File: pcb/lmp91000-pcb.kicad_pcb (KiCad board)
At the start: 2 copper layers, 48 parts, among them J1 TC2030, J2 UJC-H-G-SMT-2-P6-TR, J3 0530480210, J4 TB003-500-P03BE, J5 0528070310, J6 Conn_01x03_Pin, Q1 NTR4003N, SW1 PTS815SJM250SMTRLFS, U1 2450AT18D0100001E, U2 EFR32BG24L210F768IM40-B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

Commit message: Finish PCB
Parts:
- removed C3: 1u, Capacitor_SMD:C_0402_1005Metric
- removed J6: Conn_01x03_Pin, Connector_PinHeader_2.54mm:PinHeader_1x03_P2.54mm_Vertical
- added G***: LOGO, LOGO, F.Cu at (40.5, 58.0)
- added H1: M2, MountingHole:MountingHole_2.2mm_M2, F.Cu at (35.0, 35.0)
- added H2: M2, MountingHole:MountingHole_2.2mm_M2, F.Cu at (60.0, 35.0)
- added H3: M2, MountingHole:MountingHole_2.2mm_M2, F.Cu at (35.0, 60.0)
- added H4: M2, MountingHole:MountingHole_2.2mm_M2, F.Cu at (60.0, 60.0)
- C12: footprint Capacitor_SMD:C_0805_2012Metric -> Capacitor_SMD:C_0603_1608Metric_Pad1.08x0.95mm_HandSolder
- J3: moved to B.Cu
- J4: value TB003-500-P03BE -> TB0011-350-03GR; footprint TerminalBlock_SameSky:CUI_TB003-500-P03BE -> TerminalBlock_SameSky:SAMESKY_TB0011-350-03GR
- R12: footprint Resistor_SMD:R_0805_2012Metric -> Resistor_SMD:R_0603_1608Metric_Pad0.98x0.95mm_HandSolder
- moved J1 96.1 mm to (49.0, 60.0)
- moved C1 88.5 mm to (44.5, 44.0), turned to 90 degrees
- moved C2 88.1 mm to (45.7, 44.0), turned to 90 degrees
- moved Y1 88.0 mm to (40.0, 53.5), turned to -90 degrees
- moved FB1 86.6 mm to (42.9, 53.0), turned to -90 degrees
- moved U2 82.3 mm to (44.3, 48.5)
- moved D3 78.0 mm to (49.0, 44.0), turned to -90 degrees
- moved C6 77.4 mm to (46.9, 44.0), turned to 90 degrees
- moved R14 77.3 mm to (50.0, 44.0), turned to -90 degrees
- moved R12 67.0 mm to (50.8, 55.2), turned to 180 degrees
- moved R10 61.7 mm to (50.0, 47.0), turned to 180 degrees
- moved R11 59.1 mm to (52.0, 47.0)
- moved C12 58.4 mm to (50.8, 56.8), turned to 180 degrees
- moved U5 57.9 mm to (51.5, 50.5), turned to -90 degrees
- moved L1 54.9 mm to (43.7, 56.7), turned to 90 degrees
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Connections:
- net /IMU_INT1 renamed /IMU/INT1
- net Net-(C4-Pad2) renamed /PI
- net Net-(U1-FEED) renamed /FEED
- net Net-(U2-RF2G4_IO) renamed /RF2G4_IO
- J4 pad 1: /LMP/CE -> /LMP/RE
- J4 pad 3: /LMP/RE -> /LMP/CE
- U2 pad 1: unconnected-(U2-PC00-Pad1) -> /LDO_EN
- U2 pad 2: unconnected-(U2-PC01-Pad2) -> /PWR_BTN
- U2 pad 21: unconnected-(U2-PA00-Pad21) -> /LMP_VOUT
- U2 pad 25: unconnected-(U2-PA04-Pad25) -> /LMP_SDA
- U2 pad 26: unconnected-(U2-PA05-Pad26) -> /LMP_SCL
- U2 pad 27: unconnected-(U2-PA06-Pad27) -> /LMP_MENB
- U2 pad 29: unconnected-(U2-PA08-Pad29) -> /LED
- U2 pad 4: unconnected-(U2-PC03-Pad4) -> /IMU_SDO
- U2 pad 40: unconnected-(U2-PD00-Pad40) -> /BATT_MEAS
- U2 pad 5: unconnected-(U2-PC04-Pad5) -> /IMU_SDI
- U2 pad 6: unconnected-(U2-PC05-Pad6) -> /IMU_SPC
- U2 pad 7: unconnected-(U2-PC06-Pad7) -> /IMU_CS
- U2 pad 8: unconnected-(U2-PC07-Pad8) -> /IMU_INT2
- Y1 pad 1: /XTAL_I -> /HFXTAL_I
- Y1 pad 3: /XTAL_O -> /HFXTAL_O
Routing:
- net GND: track 0.00 -> 27.2 mm, vias 0 -> 35
- net /PWR_BTN: track 0.00 -> 25.4 mm, vias 0 -> 2
- net /LMP/RE: track 0.00 -> 21.8 mm
- net /LMP/CE: track 0.00 -> 17.8 mm
- net /LMP/WE: track 0.00 -> 17.5 mm
- net /LDO_EN: track 0.00 -> 16.0 mm, vias 0 -> 2
- net +3V3: track 0.00 -> 15.9 mm, vias 0 -> 13
- net +BATT: track 0.00 -> 15.0 mm
- net /RESETn: track 0.00 -> 14.7 mm, vias 0 -> 2
- net /SWV/SWO: track 0.00 -> 12.7 mm, vias 0 -> 2
- net /BATT_MEAS: track 0.00 -> 11.7 mm, vias 0 -> 2
- net /SWDIO: track 0.00 -> 11.3 mm, vias 0 -> 2
- net /LMP_MENB: track 0.00 -> 11.2 mm
- net VBUS: track 0.00 -> 10.7 mm
- net /SWCLK: track 0.00 -> 10.7 mm, vias 0 -> 2
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- added copper zone on F.Cu, net +3V3
- added copper zone on In2.Cu, net +3V3
- added copper zone on F.Cu, net +BATT
- added copper zone on B.Cu, net GND
- added copper zone on F.Cu, net GND
- added copper zone on In1.Cu, net GND
- added copper zone on F.Cu, net VBUS
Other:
- board outline added: 30 x 30 mm
- copper layers 2 -> 4
- board text added: "+ -"
- board text added: "3.7V Li-ion"
- board text added: "C"
- board text added: "CE WE RE"
- board text added: "EP-N"
- board text added: "M2 x4"
- board text added: "PWR"
- board text added: "R"
- board text added: "TC2030"
- board text added: "USB"

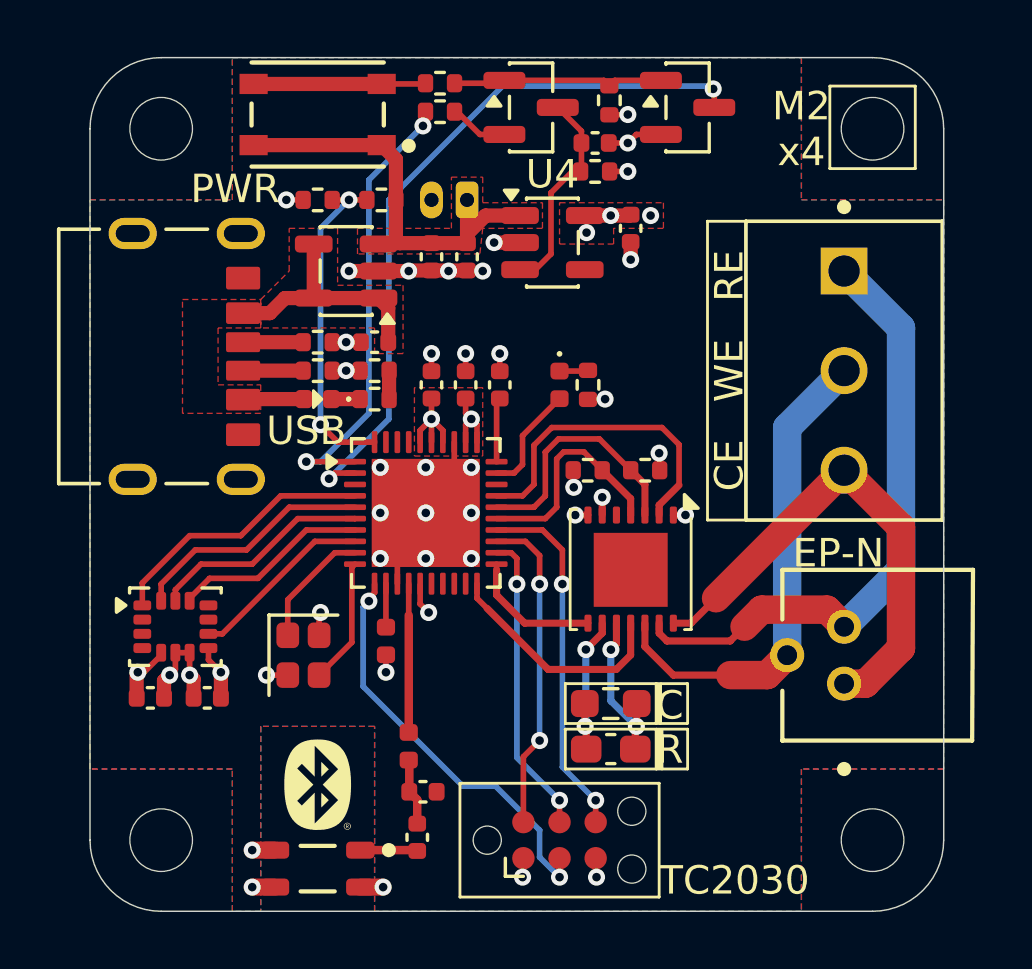
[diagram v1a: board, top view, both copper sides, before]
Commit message: Move antenna and tag connect
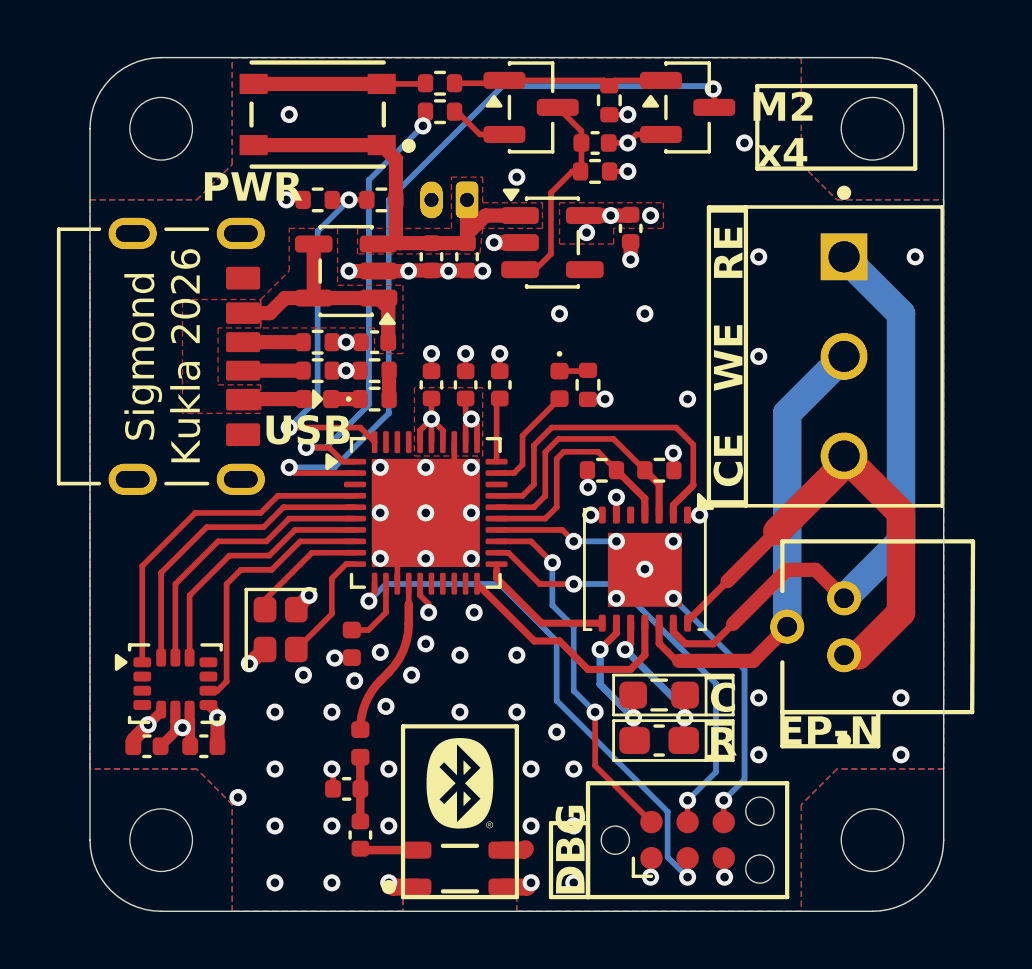
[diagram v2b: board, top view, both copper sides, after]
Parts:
- added G***: LOGO, LOGO, B.Cu at (45.5, 45.0)
- added G***: LOGO, LOGO, B.Cu at (43.5, 55.0)
- moved G*** 5.00 mm to (45.5, 58.0)
- moved U1 5.00 mm to (45.5, 61.0), turned to 0 degrees
- moved J1 4.50 mm to (53.5, 60.0)
- moved C5 2.68 mm to (41.5, 58.2), turned to 180 degrees
- moved C4 2.00 mm to (42.0, 59.8)
- moved U6 2.00 mm to (35.5, 54.5)
- moved R12 1.73 mm to (52.5, 54.9)
- moved C12 1.73 mm to (52.5, 56.5)
- moved C13 1.70 mm to (36.5, 56.7)
- moved C14 1.70 mm to (34.5, 56.7)
- moved L1 1.70 mm to (42.0, 56.6)
- moved Y1 1.20 mm to (39.2, 52.6)
- moved FB1 1.20 mm to (41.7, 53.1)
- moved J5 1.00 mm to (59.0, 53.5)
- moved J4 0.50 mm to (59.0, 43.0)
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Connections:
- net /IMU/INT1 renamed /IMU_INT1
- U1 pad 1: /FEED -> GND
- U1 pad 4: GND -> /FEED
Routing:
- net /RESETn: track 14.7 -> 19.2 mm
- net /SWCLK: track 10.7 -> 14.9 mm
- net /SWV/SWO: track 12.7 -> 16.4 mm
- net /IMU_INT2: track 6.50 -> 9.33 mm
- net /PWR_BTN: track 25.4 -> 27.9 mm
- net /IMU_SDO: track 9.53 -> 11.9 mm
- net /IMU_SDI: track 8.51 -> 10.8 mm
- net /IMU_SPC: track 7.74 -> 9.85 mm
- net /IMU_CS: track 6.89 -> 8.95 mm
- net /BATT_MEAS: track 11.7 -> 13.3 mm
- net /SWDIO: track 11.3 -> 12.8 mm
- net /LMP/WE: track 17.5 -> 16.3 mm
- net Net-(U2-RFVDD): track 1.53 -> 2.47 mm
- net /LMP/CE: track 17.8 -> 17.1 mm
- net GND: track 27.2 -> 27.9 mm, vias 35 -> 79
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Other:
- board text added: "CE"
- board text added: "DBG"
- board text added: "RE"
- board text added: "Sigmond Kukla 2026"
- board text added: "WE"
- board text added: "Wireless Potentiostat"
- board text removed: "TC2030"

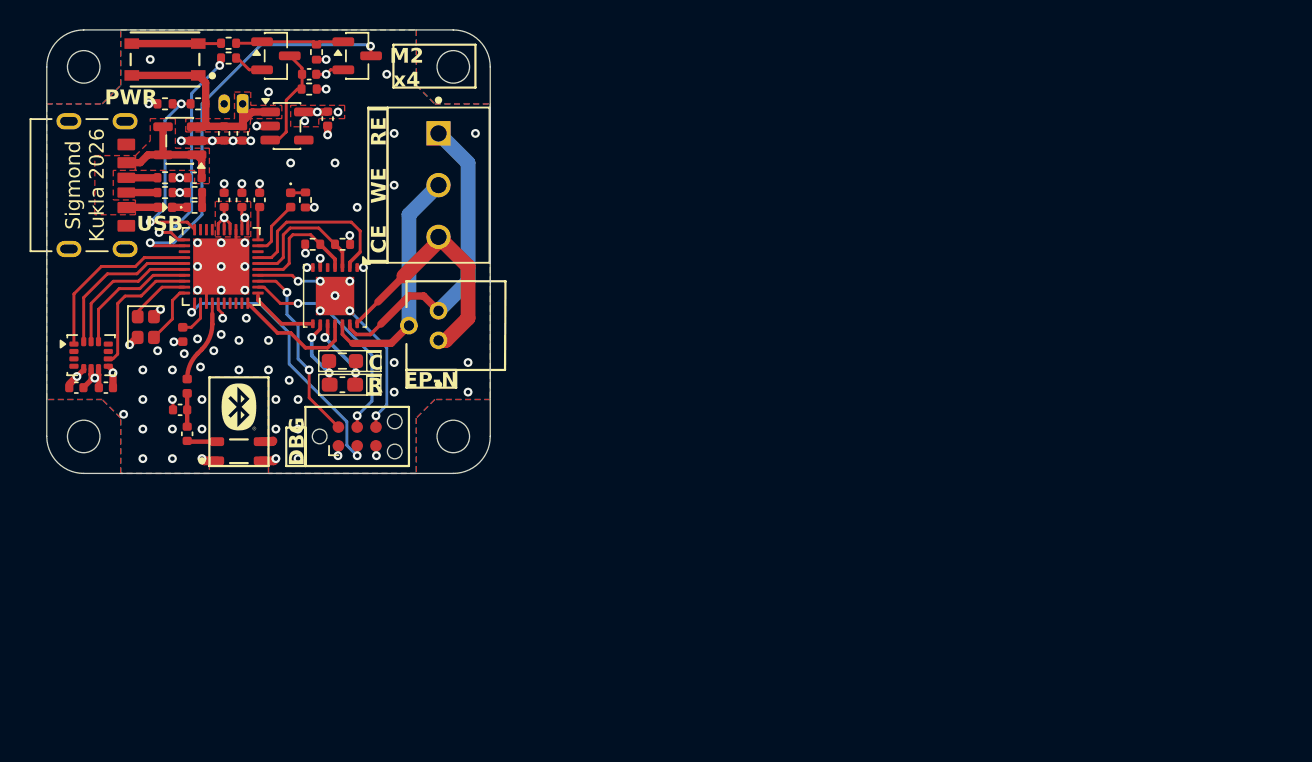
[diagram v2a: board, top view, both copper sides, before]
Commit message: Shrink PCB page and center on page
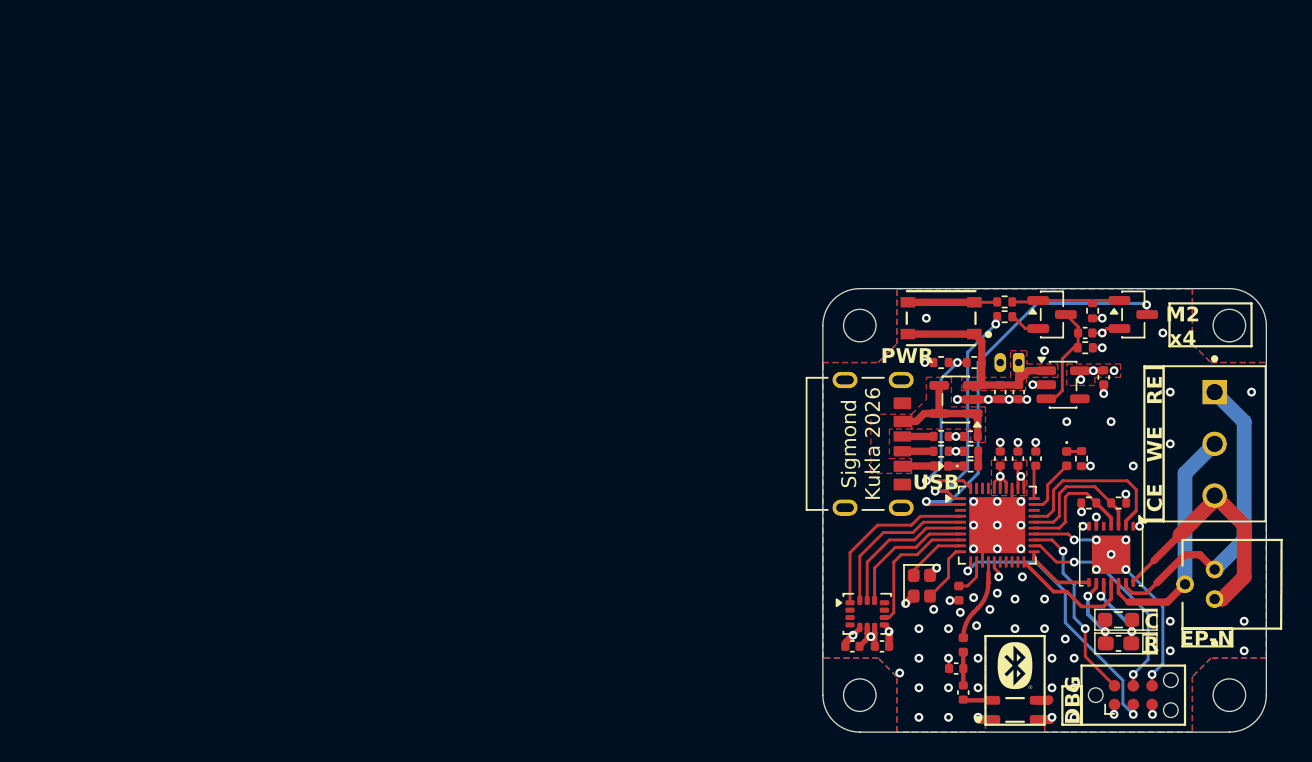
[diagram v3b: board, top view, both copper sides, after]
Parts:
- moved C6 55.3 mm to (99.4, 61.5)
- moved J5 55.3 mm to (111.5, 71.0)
- moved R10 55.3 mm to (103.0, 64.5)
- moved R8 55.3 mm to (95.2, 55.0)
- moved C1 55.3 mm to (97.0, 61.5)
- moved C10 55.3 mm to (97.0, 57.0)
- moved C11 55.3 mm to (104.0, 56.0)
- moved C12 55.3 mm to (105.0, 74.0)
- moved C13 55.3 mm to (89.0, 74.2)
- moved C14 55.3 mm to (87.0, 74.2)
- moved C2 55.3 mm to (98.2, 61.5)
- moved C7 55.3 mm to (102.8, 53.0)
- moved C8 55.3 mm to (98.2, 57.0)
- moved C9 55.3 mm to (95.0, 60.0)
- moved D1 55.3 mm to (100.5, 51.8)
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
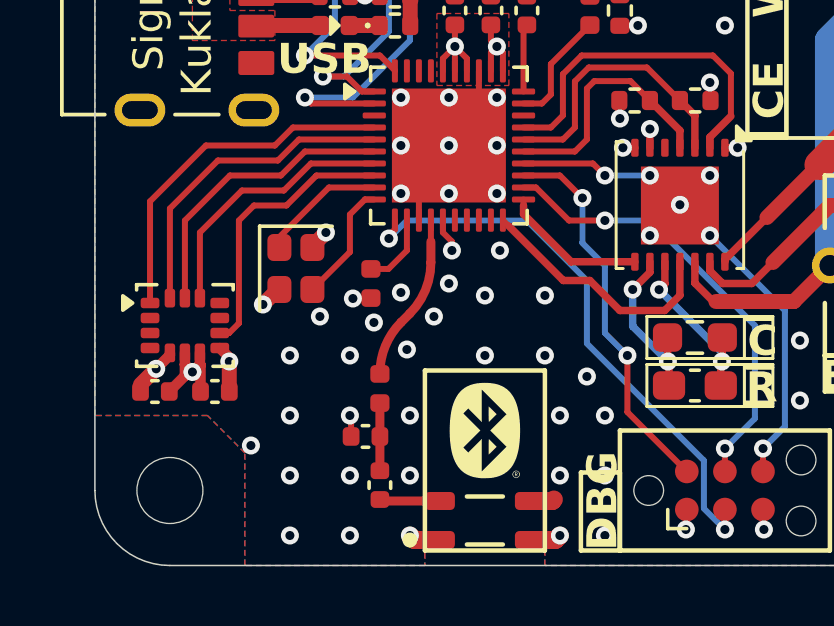
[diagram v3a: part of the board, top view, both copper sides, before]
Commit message: Adjust RF trace grounding
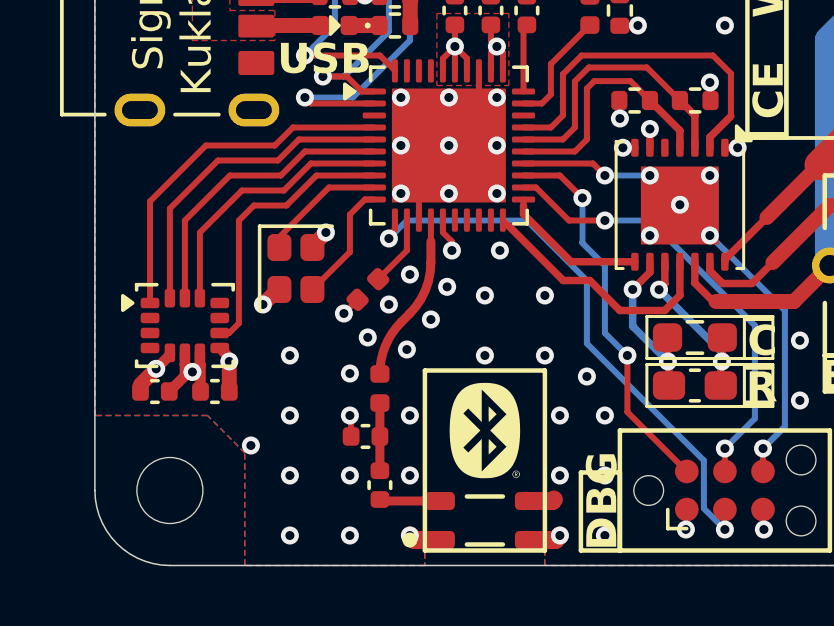
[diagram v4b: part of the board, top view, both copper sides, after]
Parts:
- moved FB1 0.22 mm to (94.1, 70.8), turned to -135 degrees

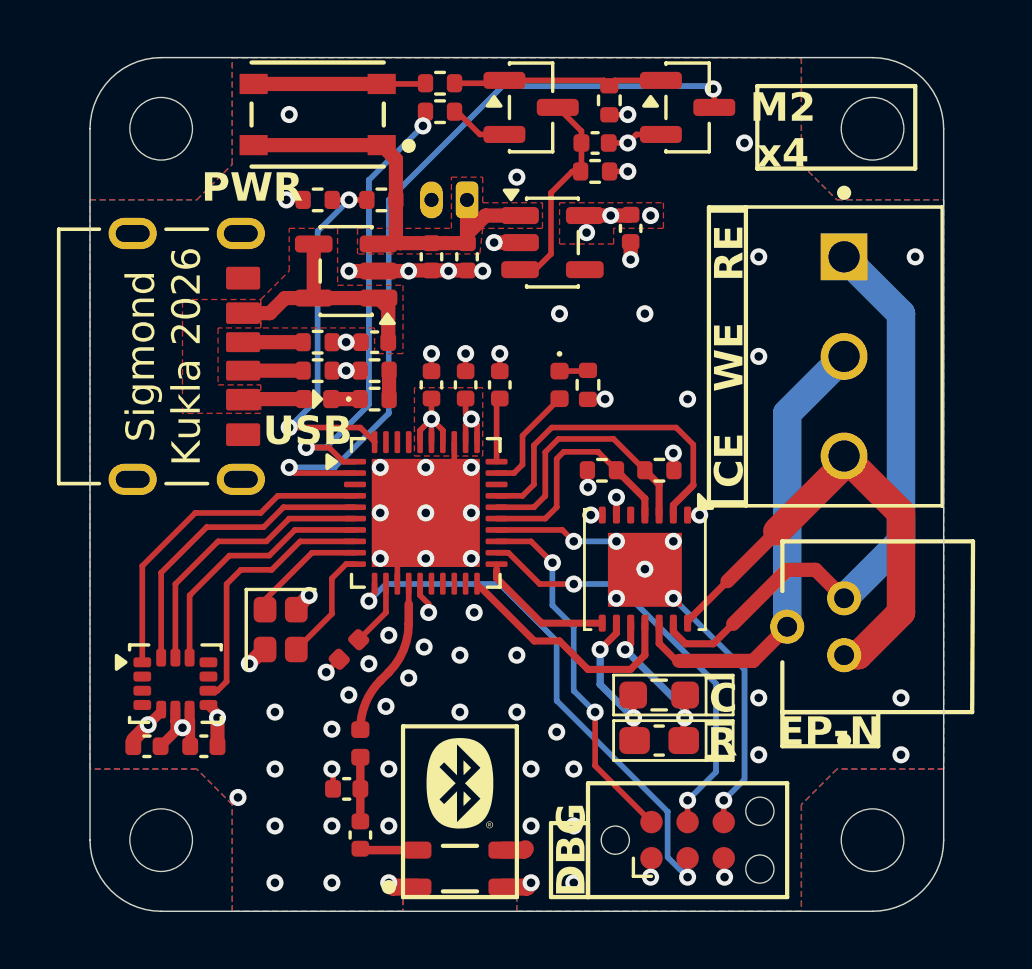
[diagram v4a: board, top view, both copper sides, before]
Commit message: Cleaned up routing
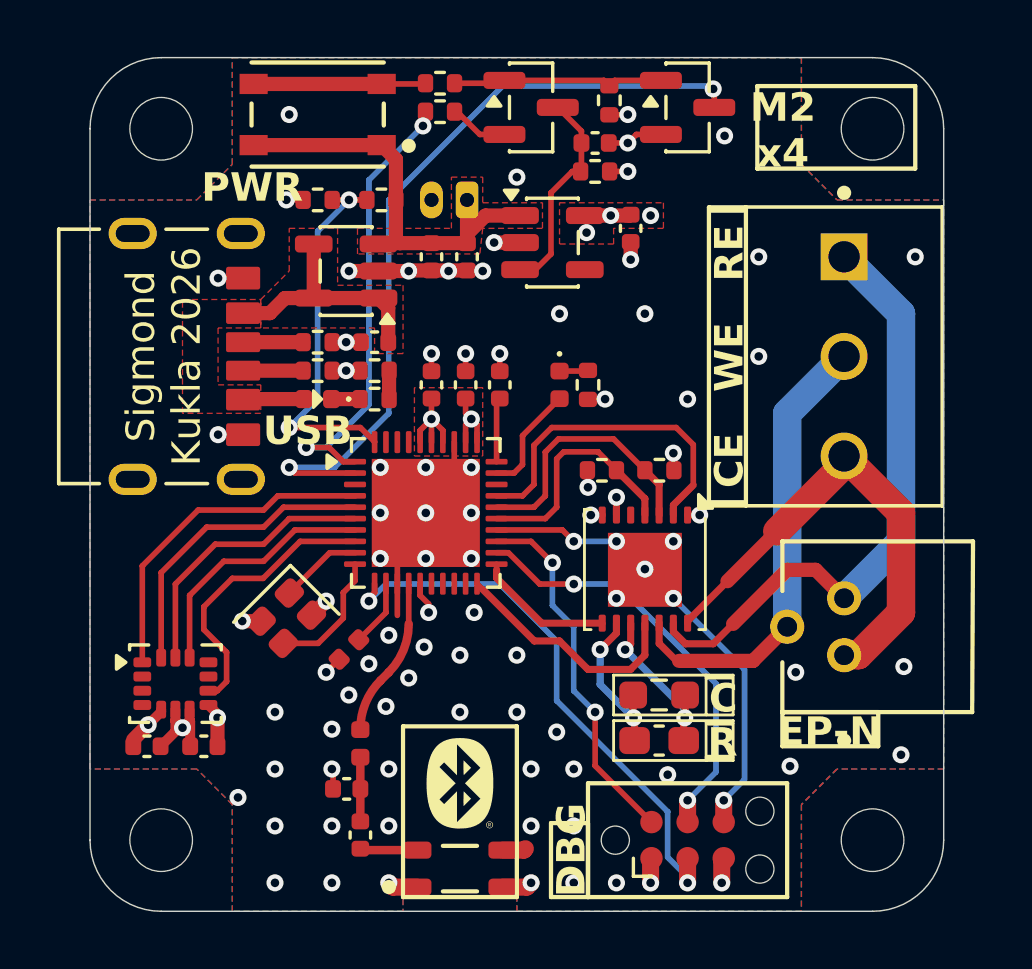
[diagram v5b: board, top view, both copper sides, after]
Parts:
- moved Y1 0.45 mm to (91.9, 69.7), turned to -135 degrees
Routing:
- net /HFXTAL_I: track 4.20 -> 2.89 mm
- net GND: track 27.9 -> 29.2 mm, vias 79 -> 83
- net /IMU_INT2: track 9.33 -> 9.99 mm
- net /HFXTAL_O: track 4.04 -> 4.54 mm

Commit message: Run DRC
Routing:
- net /SWCLK: track 14.9 -> 15.4 mm
- net GND: vias 83 -> 80
